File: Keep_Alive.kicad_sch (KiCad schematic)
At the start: 7 parts, among them IC1 PSM712-LF-T7, U41 MIC5205-3.3YM5

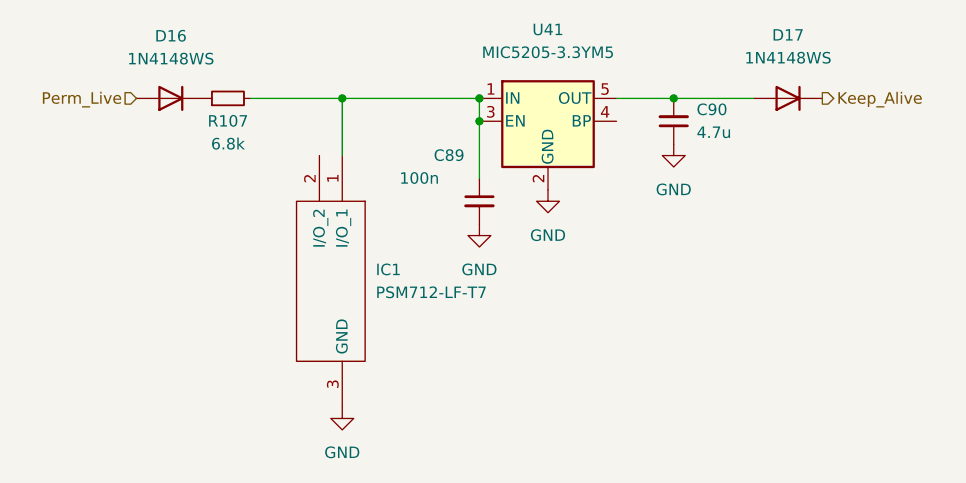
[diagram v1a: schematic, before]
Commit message: make hardware updates: - fix erc/drc errors - switch to VNLD5090 - switch to SOIC8 ignition drivers - BOM deduplication of similar parts
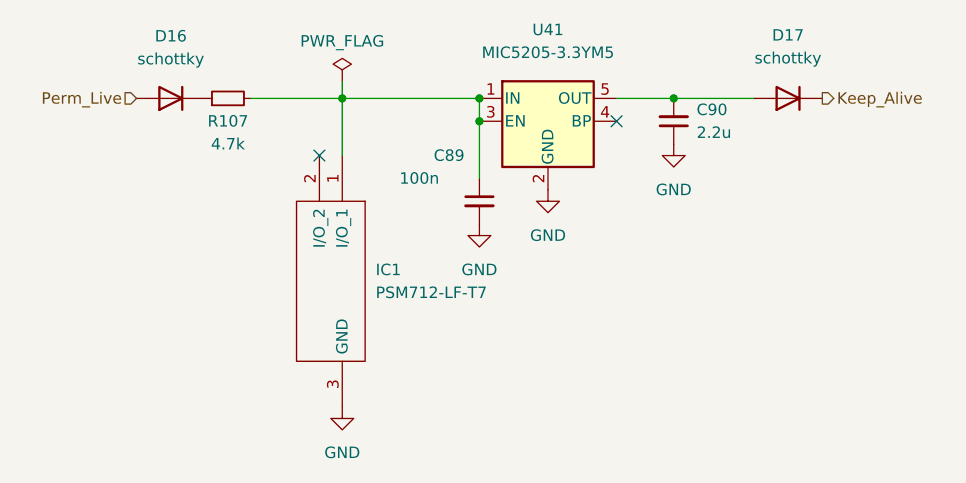
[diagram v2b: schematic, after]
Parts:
- C89: footprint Capacitor_SMD:C_0805_2012Metric -> Capacitor_SMD:C_0603_1608Metric; LCSC (none) -> C14663
- C90: value 4.7u -> 2.2u; footprint Capacitor_SMD:C_0805_2012Metric -> Capacitor_SMD:C_0603_1608Metric; LCSC (none) -> C23630
- D16, D17: value 1N4148WS -> schottky; footprint Diode_SMD:D_SOD-323 -> Diode_SMD:D_SOD-123; LCSC (none) -> C8598
- IC1: LCSC (none) -> C32677
- R107: value 6.8k -> 4.7k; LCSC (none) -> C17673
- U41: LCSC (none) -> C5370979
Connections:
- no-connect marks 0 -> 2
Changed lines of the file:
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@@
   (junction (at 127 73.66) (diameter 0) (color 0 0 0 0)
   )
+  (no_connect (at 120.65 76.2))
+  (no_connect (at 87.63 80.01))
   (wire (pts (xy 120.65 73.66) (xy 127 73.66))
     (stroke (width 0) (type default))
@@
   )
   (wire (pts (xy 127 73.66) (xy 135.89 73.66))
+    (stroke (width 0) (type default))
+  )
+  (wire (pts (xy 90.17 71.755) (xy 90.17 73.66))
     (stroke (width 0) (type default))
   )
@@
       (effects (font (size 1.27 1.27)) (justify left) hide)
     )
+    (property "LCSC" "C32677" (at 90.17 80.01 0)
+      (effects (font (size 1.27 1.27)) hide)
+    )
     (pin "1")
     (pin "2")
@@
     )
     (property "Datasheet" "http://ww1.microchip.com/downloads/en/DeviceDoc/20005785A.pdf" (at 113.03 76.2 0)
+      (effects (font (size 1.27 1.27)) hide)
+    )
+    (property "LCSC" "C5370979" (at 113.03 76.2 0)
       (effects (font (size 1.27 1.27)) hide)
     )
@@
       (effects (font (size 1.27 1.27)) (justify right))
     )
-    (property "Value" "4.7u" (at 129.54 77.4635 0)
+    (property "Value" "2.2u" (at 129.54 77.4635 0)
       (effects (font (size 1.27 1.27)) (justify right))
     )
-    (property "Footprint" "Capacitor_SMD:C_0805_2012Metric" (at 127 76.2 0)
+    (property "Footprint" "Capacitor_SMD:C_0603_1608Metric" (at 127 76.2 0)
       (effects (font (size 1.27 1.27)) hide)
     )
@@
       (effects (font (size 1.27 1.27)) hide)
     )
+    (property "LCSC" "C23630" (at 127 76.2 0)
+      (effects (font (size 1.27 1.27)) hide)
+    )
     (pin "1")
     (pin "2")
@@
       (effects (font (size 1.27 1.27)))
     )
-    (property "Value" "1N4148WS" (at 139.7 69.1885 0)
-      (effects (font (size 1.27 1.27)))
-    )
-    (property "Footprint" "Diode_SMD:D_SOD-323" (at 139.7 69.215 0)
+    (property "Value" "schottky" (at 139.7 69.1885 0)
+      (effects (font (size 1.27 1.27)))
+    )
+    (property "Footprint" "Diode_SMD:D_SOD-123" (at 139.7 69.215 0)
       (effects (font (size 1.27 1.27)) hide)
     )
     (property "Datasheet" "https://www.vishay.com/docs/85751/1n4148ws.pdf" (at 139.7 73.66 0)
+      (effects (font (size 1.27 1.27)) hide)
+    )
+    (property "LCSC" "C8598" (at 139.7 73.66 0)
       (effects (font (size 1.27 1.27)) hide)
     )
@@
       (effects (font (size 1.27 1.27)))
     )
-    (property "Value" "6.8k" (at 77.47 78.74 90)
+    (property "Value" "4.7k" (at 77.47 78.74 90)
       (effects (font (size 1.27 1.27)))
     )
@@
     )
     (property "Datasheet" "~" (at 77.47 73.66 0)
+      (effects (font (size 1.27 1.27)) hide)
+    )
+    (property "LCSC" "C17673" (at 77.47 73.66 0)
       (effects (font (size 1.27 1.27)) hide)
     )
@@
       (effects (font (size 1.27 1.27)) (justify left))
     )
-    (property "Footprint" "Capacitor_SMD:C_0805_2012Metric" (at 105.41 85.09 0)
+    (property "Footprint" "Capacitor_SMD:C_0603_1608Metric" (at 105.41 85.09 0)
       (effects (font (size 1.27 1.27)) hide)
     )
@@
       (effects (font (size 1.27 1.27)) hide)
     )
+    (property "LCSC" "C14663" (at 105.41 85.09 0)
+      (effects (font (size 1.27 1.27)) hide)
+    )
     (pin "1")
     (pin "2")
@@
       (effects (font (size 1.27 1.27)))
     )
-    (property "Value" "1N4148WS" (at 71.12 69.2882 0)
-      (effects (font (size 1.27 1.27)))
-    )
-    (property "Footprint" "Diode_SMD:D_SOD-323" (at 71.12 69.215 0)
+    (property "Value" "schottky" (at 71.12 69.2882 0)
+      (effects (font (size 1.27 1.27)))
+    )
+    (property "Footprint" "Diode_SMD:D_SOD-123" (at 71.12 69.215 0)
       (effects (font (size 1.27 1.27)) hide)
     )
@@
       (effects (font (size 1.27 1.27)) hide)
     )
+    (property "LCSC" "C8598" (at 71.12 73.66 0)
+      (effects (font (size 1.27 1.27)) hide)
+    )
     (pin "1")
     (pin "2")
@@
         )
       )
+    )
+  )
+  (symbol (lib_id "power:PWR_FLAG") (at 90.17 71.755 0) (unit 1)
+    (in_bom yes) (on_board yes) (dnp no) (fields_autoplaced)
+    (property "Reference" "#FLG01401" (at 90.17 69.85 0)
+      (effects (font (size 1.27 1.27)) hide)
+    )
+    (property "Value" "PWR_FLAG" (at 90.17 67.31 0)
+      (effects (font (size 1.27 1.27)))
+    )
+    (property "Footprint" "" (at 90.17 71.755 0)
+      (effects (font (size 1.27 1.27)) hide)
+    )
+    (property "Datasheet" "~" (at 90.17 71.755 0)
+      (effects (font (size 1.27 1.27)) hide)
+    )
+    (pin "1")
+    (instances
+      (project "polygonus-Shortage-Version"
+        (path "/3b9c5ffd-e59b-402d-8c5e-052f7ca643a4/46495fed-359e-4c30-808a-9217af090de7"
+          (reference "#FLG01401") (unit 1)
+        )
+      )
